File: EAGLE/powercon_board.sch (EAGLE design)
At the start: 68 parts, among them CN1 POWER_IF, CN2 PICkit_IF, CN3 ROTARY_ENCODER, CN4 FEEDER_IF, Q1 2SC1815, Q2 2N7000, Q3 2SC1815, Q4 2SK2232, SW1 10-XX, SW2 10-XX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

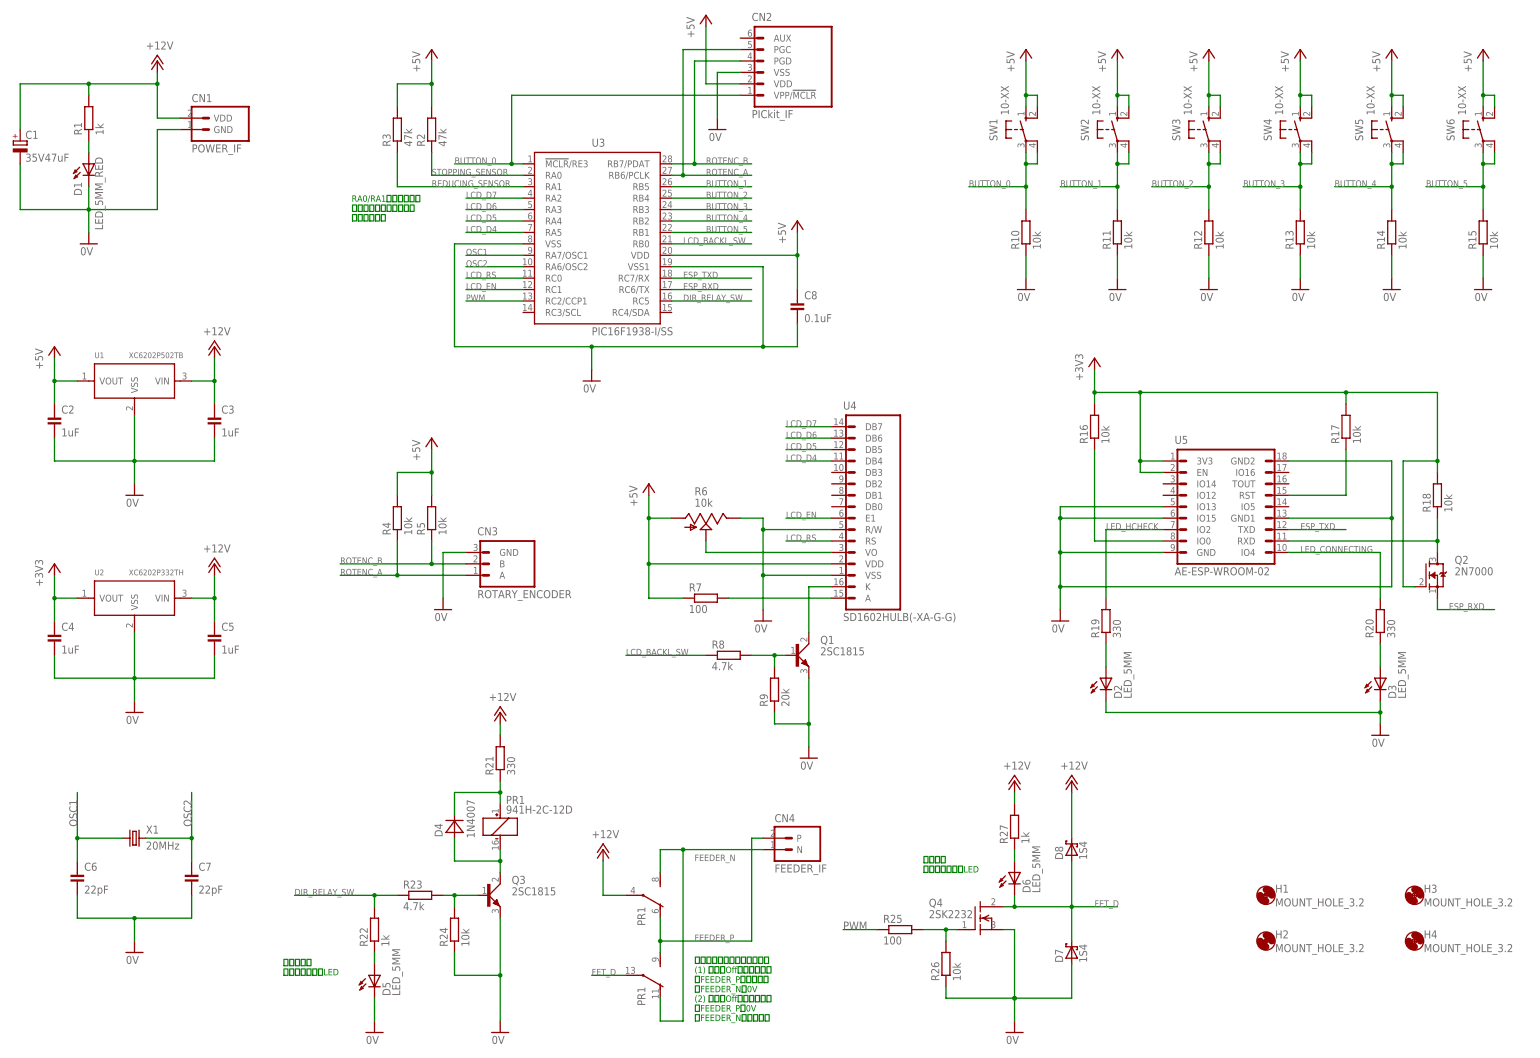
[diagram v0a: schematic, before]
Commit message: Wi-Fi部が不要になったため回路図から削除
別途作成のWi-Fi HTTP通信基板に接続する前提
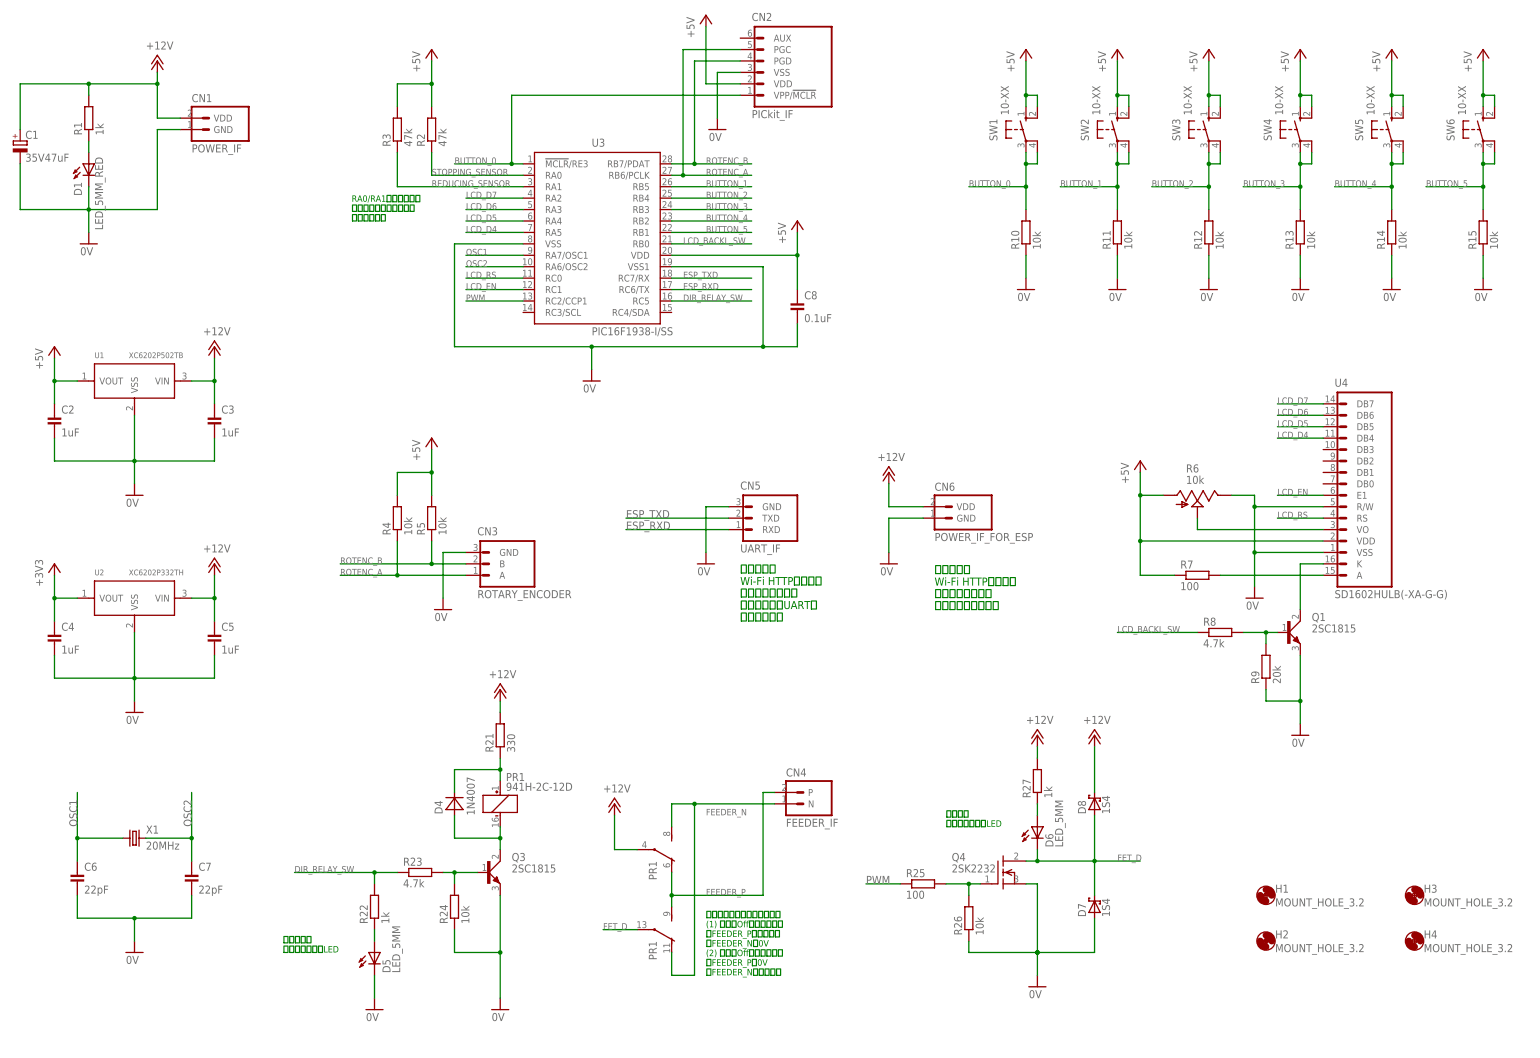
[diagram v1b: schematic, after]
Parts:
- removed D2, D3: LED_5MM, Parts:LED_5MM
- removed Q2: 2N7000, Parts:2N7000
- removed R16, R17, R18: 10k, Parts:RESISTOR_300MIL
- removed R19, R20: 330, Parts:RESISTOR_300MIL
- removed U5: AE-ESP-WROOM-02, PartsForProto:AE-ESP-WROOM-02
- added CN5: UART_IF, PartsForProto:UART_IF
- added CN6: POWER_IF_FOR_ESP, PartsForProto:POWER_IF
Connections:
- removed net LED_CONNECTING: R20.2, U5.IO4
- removed net LED_HCHECK: R19.2, U5.IO2
- removed net N$10: R17.1, U5.RST
- removed net N$11: D3.A, R20.1
- removed net N$12: D2.A, R19.1
- removed net N$7: Q2.D, R18.1, U5.RXD
- removed net N$9: R16.1, U5.IO0
- net +12V: now also CN6.VDD
- net +3V3: no longer Q2.G, R16.2, R17.2, R18.2, U5.3V3, U5.EN
- net 0V: now also CN5.GND, CN6.GND; no longer D2.C, D3.C, U5.GND, U5.GND1, U5.GND2, U5.IO13, U5.IO15
- net ESP_RXD: now also CN5.RXD; no longer Q2.S
- net ESP_TXD: now also CN5.TXD; no longer U5.TXD
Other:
- note added: "別途作成の Wi-Fi HTTP通信基板 （親機モード）の ソフトウェアUARTに 接続します。"
- note added: "別途作成の Wi-Fi HTTP通信基板 （親機モード）へ 電源を供給します。"
- moved on the sheet: CN4, D4, D5, D6, D7, D8, PR1, Q1, Q3, Q4, R21, R22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
